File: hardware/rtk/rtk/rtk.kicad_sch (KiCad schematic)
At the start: 0 parts

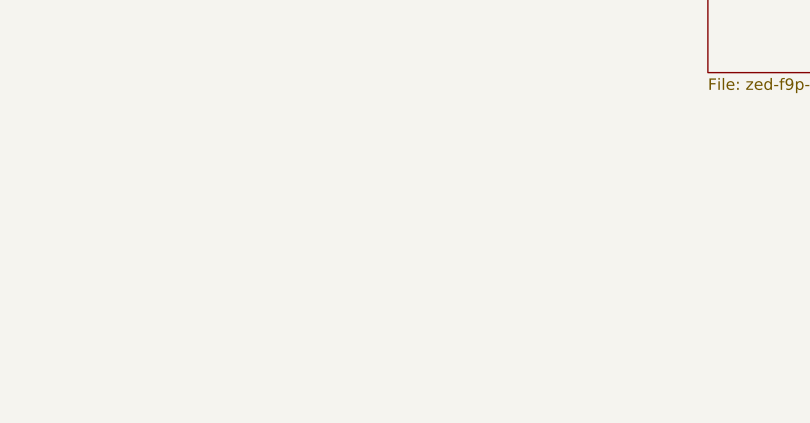
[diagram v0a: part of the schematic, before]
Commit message: Hardware schematic progress: F765 pin assignments, USB HS, TCXO (#182)
- STM32F765VIT pin assignments via CubeMX (rtk-base.ioc updated)
- USB HS hierarchical sheet added (usb2hs.kicad_sch): USB3300 ULPI PHY,
  all 13 ULPI signals wired, reset GPIO, SOF test point
- ASTX-H11-16.000MHZ-T TCXO symbol + footprint added
- USB3300-EZK-TR symbol + footprint added
- USB3300-EZK-TR datasheet added to docs/datasheets/ + catalog updated
- PSU, STM32, ZED-F9P schematic sheets updated
- docs/reference/psu/README.md BQ24075 entry included

Co-Authored-By: Claude Sonnet 4.6 <noreply@anthropic.com>
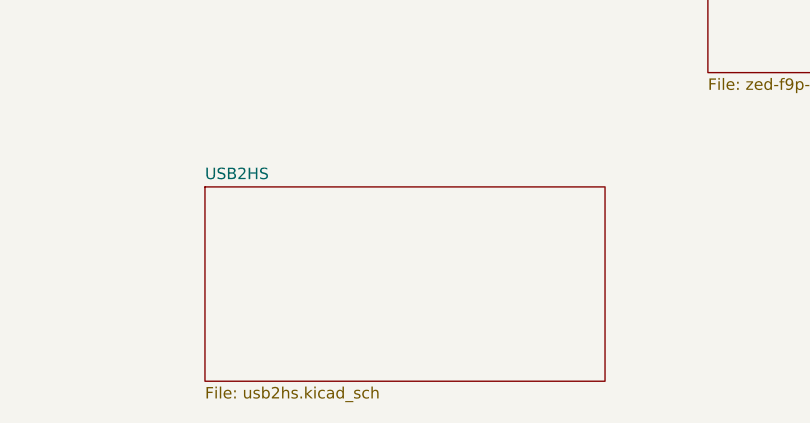
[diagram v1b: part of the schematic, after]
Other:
- added sheet USB2HS (usb2hs.kicad_sch)
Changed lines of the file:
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@@
+	)
+	(sheet
+		(at 64.77 147.32)
+		(size 44.45 21.59)
+		(exclude_from_sim no)
+		(in_bom yes)
+		(on_board yes)
+		(dnp no)
+		(fields_autoplaced yes)
+		(stroke
+			(width 0.1524)
+			(type solid)
+		)
+		(fill
+			(color 0 0 0 0)
+		)
+		(property "Sheetname" "USB2HS"
+			(at 64.77 146.6084 0)
+			(show_name no)
+			(do_not_autoplace no)
+			(effects
+				(font
+					(size 1.27 1.27)
+				)
+				(justify left bottom)
+			)
+		)
+		(property "Sheetfile" "usb2hs.kicad_sch"
+			(at 64.77 169.4946 0)
+			(show_name no)
+			(do_not_autoplace no)
+			(effects
+				(font
+					(size 1.27 1.27)
+				)
+				(justify left top)
+			)
+		)
+		(instances
+			(project "rtk"
+				(path "/608e0f5f-bf55-4b10-9802-aab1430116aa"
+					(page "5")
+				)
+			)
+		)
 	)
 	(sheet

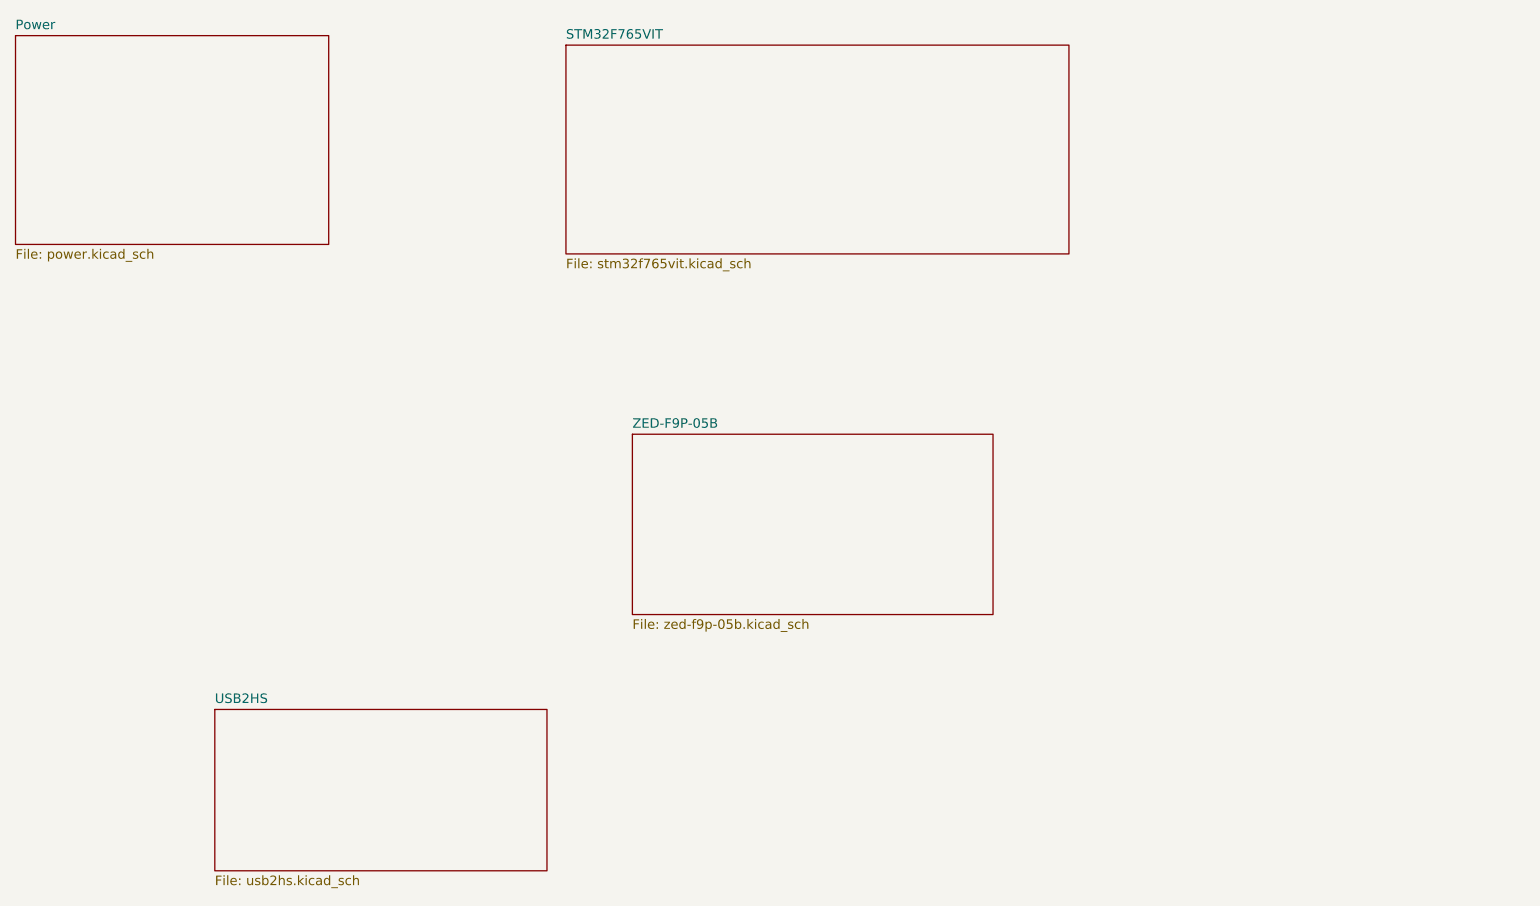
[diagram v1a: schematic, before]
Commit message: Power sheet review fixes; SLVA553 inrush mitigation added (#182)
- power.kicad_sch: CC1/CC2 5.1k pull-downs on J1+J2, FB divider wiring
  fixed, TPS63020 inrush D1+C_SS per SLVA553, 1M NF bleed resistor
  across C_SS, TS NF 82k5 resistor added, nPGOOD/nCHG net labels added
- stm32f765vit.kicad_sch: nPGOOD→PD10, nCHG→PD11, SYSOFF→PD7 inputs added
- firmware/rtk-base/rtk-base.ioc: PD7/PD10/PD11 assigned
- docs/datasheets/slva553.pdf: TI SLVA553 app note (TPS6302x inrush)

Co-Authored-By: Claude Sonnet 4.6 <noreply@anthropic.com>
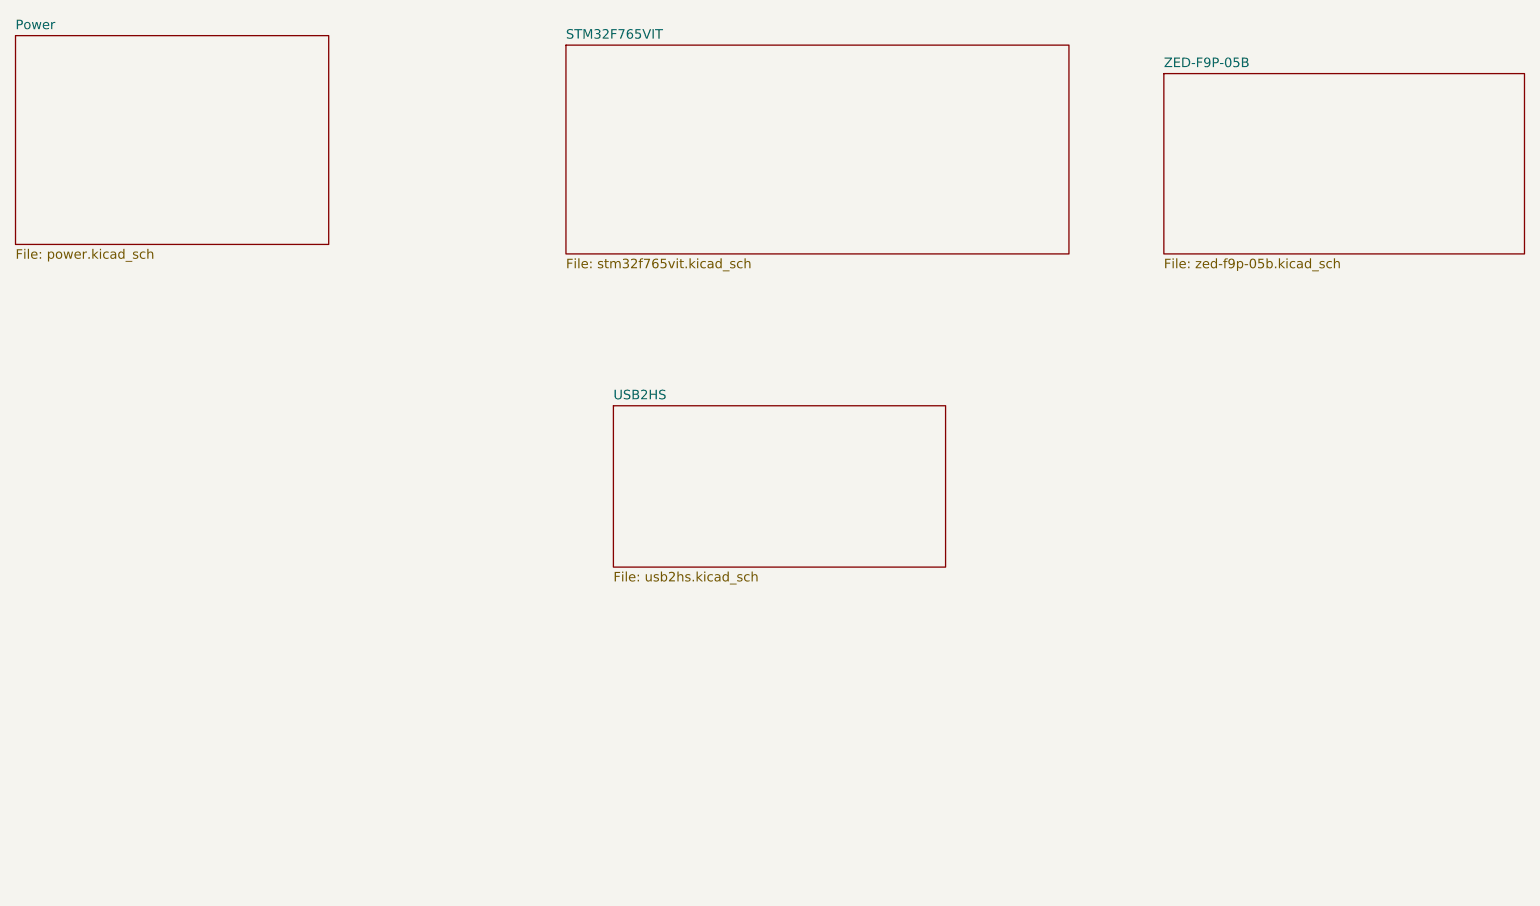
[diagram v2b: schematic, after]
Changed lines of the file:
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@@
 	(paper "A4")
 	(sheet
-		(at 120.65 110.49)
+		(at 191.77 62.23)
 		(size 48.26 24.13)
 		(exclude_from_sim no)
@@
 		)
 		(property "Sheetname" "ZED-F9P-05B"
-			(at 120.65 109.7784 0)
+			(at 191.77 61.5184 0)
 			(show_name no)
 			(do_not_autoplace no)
@@
 		)
 		(property "Sheetfile" "zed-f9p-05b.kicad_sch"
-			(at 120.65 135.2046 0)
+			(at 191.77 86.9446 0)
 			(show_name no)
 			(do_not_autoplace no)
@@
 	)
 	(sheet
-		(at 64.77 147.32)
+		(at 118.11 106.68)
 		(size 44.45 21.59)
 		(exclude_from_sim no)
@@
 		)
 		(property "Sheetname" "USB2HS"
-			(at 64.77 146.6084 0)
+			(at 118.11 105.9684 0)
 			(show_name no)
 			(do_not_autoplace no)
@@
 		)
 		(property "Sheetfile" "usb2hs.kicad_sch"
-			(at 64.77 169.4946 0)
+			(at 118.11 128.8546 0)
 			(show_name no)
 			(do_not_autoplace no)
